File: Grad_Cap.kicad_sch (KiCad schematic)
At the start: 2 parts, among them U1 Itsy_NRF

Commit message: update part
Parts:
- U1: footprint (none) -> Package_DIP:DIP-28_W15.24mm_LongPads
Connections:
- net GND: now also U1.27 (GND); no longer U1. (VHI)
- net VBUS: now also U1.28 (VBAT); no longer U1. (VHI)
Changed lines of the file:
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@@
     (property "Reference" "U1" (id 0) (at 40.64 19.05 0))
     (property "Value" "Itsy_NRF" (id 1) (at 40.64 21.59 0))
-    (property "Footprint" "" (id 2) (at 29.21 26.67 0)
+    (property "Footprint" "Package_DIP:DIP-28_W15.24mm_LongPads" (id 2) (at 29.21 26.67 0)
       (effects (font (size 1.27 1.27)) hide)
     )
@@
       (effects (font (size 1.27 1.27)) hide)
     )
-    (pin "")
-    (pin "")
-    (pin "")
-    (pin "")
-    (pin "")
-    (pin "")
-    (pin "")
-    (pin "")
-    (pin "")
-    (pin "")
-    (pin "")
-    (pin "")
-    (pin "")
-    (pin "")
-    (pin "")
-    (pin "")
-    (pin "")
-    (pin "")
-    (pin "")
-    (pin "")
-    (pin "")
-    (pin "")
-    (pin "")
-    (pin "")
-    (pin "")
-    (pin "")
-    (pin "")
-    (pin "")
+    (pin "1")
+    (pin "10")
+    (pin "11")
+    (pin "12")
+    (pin "13")
+    (pin "14")
+    (pin "15")
+    (pin "16")
+    (pin "17")
+    (pin "18")
+    (pin "19")
+    (pin "2")
+    (pin "20")
+    (pin "21")
+    (pin "22")
+    (pin "23")
+    (pin "24")
+    (pin "25")
+    (pin "26")
+    (pin "27")
+    (pin "28")
+    (pin "3")
+    (pin "4")
+    (pin "5")
+    (pin "6")
+    (pin "7")
+    (pin "8")
+    (pin "9")
   )
   (symbol (lib_id "LED:Inolux_IN-PI554FCH") (at 147.32 31.75 0) (unit 1)
@@
     )
     (path "/a5c46b29-3091-45c4-b411-8345b67a7d70"
-      (reference "U1") (unit 1) (value "Itsy_NRF") (footprint "")
+      (reference "U1") (unit 1) (value "Itsy_NRF") (footprint "Package_DIP:DIP-28_W15.24mm_LongPads")
     )
   )

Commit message: Cleaning files
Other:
- company: (none) -> Lala
- title: (none) -> Graduation Cap
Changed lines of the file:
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@@
 (kicad_sch (version 20211123) (generator eeschema)
   (paper "A4")
+  (title_block
+    (title "Graduation Cap")
+    (date "2022-12-23")
+    (rev "1.0")
+    (company "Lala")
+  )
   (wire (pts (xy 147.32 39.37) (xy 147.32 40.64))
     (stroke (width 0) (type default) (color 0 0 0 0))

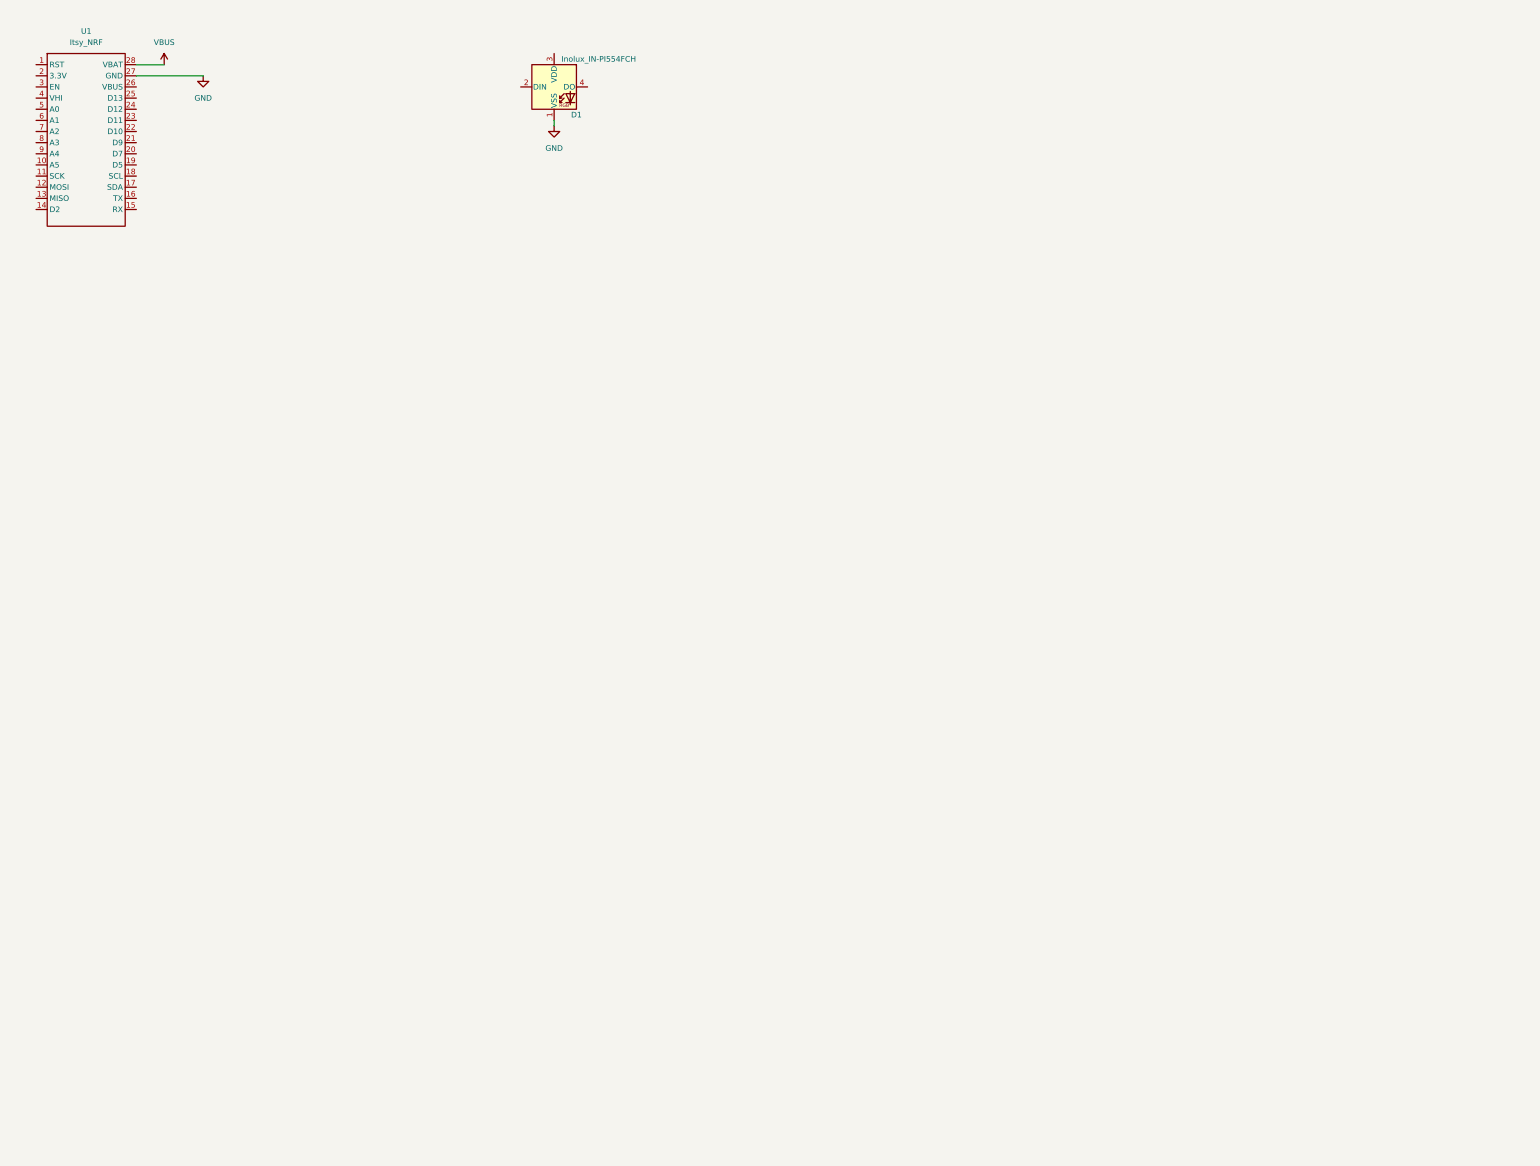
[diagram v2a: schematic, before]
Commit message: Added neopixels
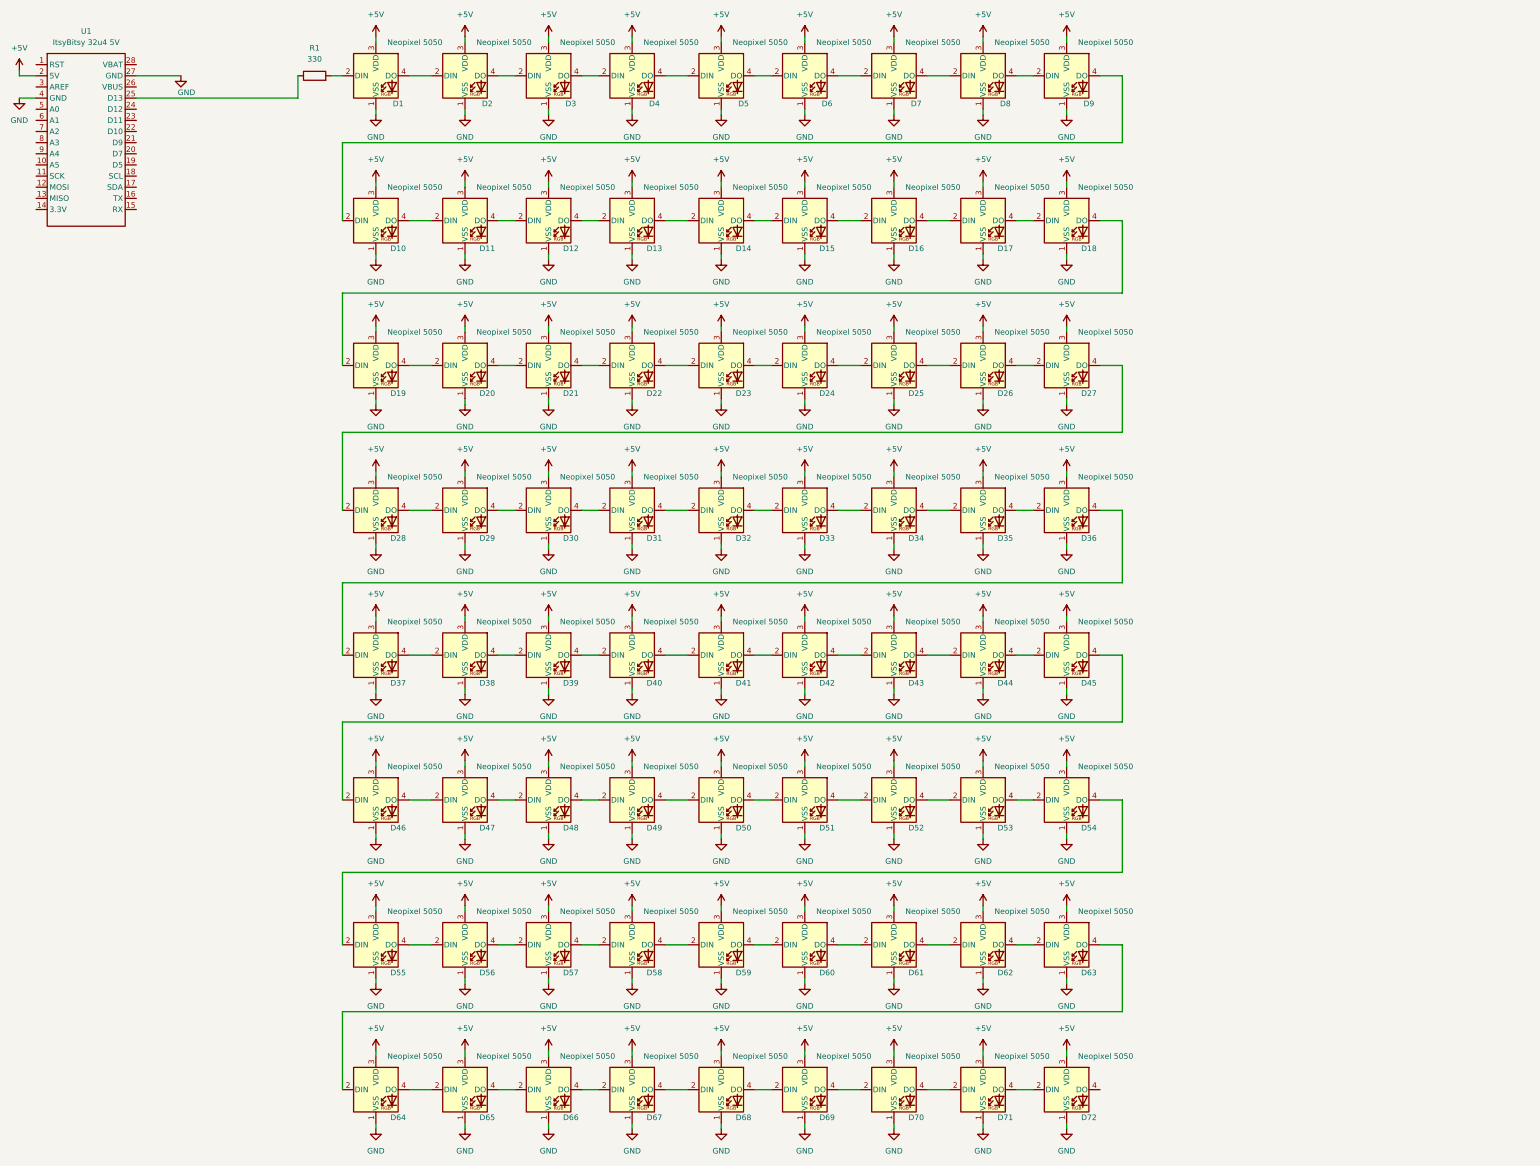
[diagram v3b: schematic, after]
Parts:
- added D10, D11, D12, D13, D14, D15, D16, D17, D18, D19, D2, D20, D21, D22, D23, D24, D25, D26, D27, D28, D29, D3, D30, D31, D32, D33, D34, D35, D36, D37, D38, D39, D4, D40, D41, D42, D43, D44, D45, D46, D47, D48, D49, D5, D50, D51, D52, D53, D54, D55, D56, D57, D58, D59, D6, D60, D61, D62, D63, D64, D65, D66, D67, D68, D69, D7, D70, D71, D72, D8, D9: Neopixel 5050, LED_SMD:LED_Inolux_IN-PI554FCH_PLCC4_5.0x5.0mm_P3.2mm, symbol LED:Inolux_IN-PI554FCH
- added R1: 330, Resistor_SMD:R_1206_3216Metric_Pad1.30x1.75mm_HandSolder, symbol Device:R
- D1: value Inolux_IN-PI554FCH -> Neopixel 5050
- U1: value Itsy_NRF -> ItsyBitsy 32u4 5V
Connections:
- net GND: now also U1.4 (GND), D10.1 (VSS), D11.1 (VSS), D12.1 (VSS), D13.1 (VSS), D14.1 (VSS), D15.1 (VSS), D16.1 (VSS), D17.1 (VSS), D18.1 (VSS), D19.1 (VSS), D2.1 (VSS), D20.1 (VSS), D21.1 (VSS), D22.1 (VSS), D23.1 (VSS), D24.1 (VSS), D25.1 (VSS), D26.1 (VSS), D27.1 (VSS), D28.1 (VSS), D29.1 (VSS), D3.1 (VSS), D30.1 (VSS), D31.1 (VSS), D32.1 (VSS), D33.1 (VSS), D34.1 (VSS), D35.1 (VSS), D36.1 (VSS), D37.1 (VSS), D38.1 (VSS), D39.1 (VSS), D4.1 (VSS), D40.1 (VSS), D41.1 (VSS), D42.1 (VSS), D43.1 (VSS), D44.1 (VSS), D45.1 (VSS), D46.1 (VSS), D47.1 (VSS), D48.1 (VSS), D49.1 (VSS), D5.1 (VSS), D50.1 (VSS), D51.1 (VSS), D52.1 (VSS), D53.1 (VSS), D54.1 (VSS), D55.1 (VSS), D56.1 (VSS), D57.1 (VSS), D58.1 (VSS), D59.1 (VSS), D6.1 (VSS), D60.1 (VSS), D61.1 (VSS), D62.1 (VSS), D63.1 (VSS), D64.1 (VSS), D65.1 (VSS), D66.1 (VSS), D67.1 (VSS), D68.1 (VSS), D69.1 (VSS), D7.1 (VSS), D70.1 (VSS), D71.1 (VSS), D72.1 (VSS), D8.1 (VSS), D9.1 (VSS)
- net +5V: now reaches U1.2 (5V)
- net +5V: now also D1.3 (VDD), D10.3 (VDD), D11.3 (VDD), D12.3 (VDD), D13.3 (VDD), D14.3 (VDD), D15.3 (VDD), D16.3 (VDD), D17.3 (VDD), D18.3 (VDD), D19.3 (VDD), D2.3 (VDD), D20.3 (VDD), D21.3 (VDD), D22.3 (VDD), D23.3 (VDD), D24.3 (VDD), D25.3 (VDD), D26.3 (VDD), D27.3 (VDD), D28.3 (VDD), D29.3 (VDD), D3.3 (VDD), D30.3 (VDD), D31.3 (VDD), D32.3 (VDD), D33.3 (VDD), D34.3 (VDD), D35.3 (VDD), D36.3 (VDD), D37.3 (VDD), D38.3 (VDD), D39.3 (VDD), D4.3 (VDD), D40.3 (VDD), D41.3 (VDD), D42.3 (VDD), D43.3 (VDD), D44.3 (VDD), D45.3 (VDD), D46.3 (VDD), D47.3 (VDD), D48.3 (VDD), D49.3 (VDD), D5.3 (VDD), D50.3 (VDD), D51.3 (VDD), D52.3 (VDD), D53.3 (VDD), D54.3 (VDD), D55.3 (VDD), D56.3 (VDD), D57.3 (VDD), D58.3 (VDD), D59.3 (VDD), D6.3 (VDD), D60.3 (VDD), D61.3 (VDD), D62.3 (VDD), D63.3 (VDD), D64.3 (VDD), D65.3 (VDD), D66.3 (VDD), D67.3 (VDD), D68.3 (VDD), D69.3 (VDD), D7.3 (VDD), D70.3 (VDD), D71.3 (VDD), D72.3 (VDD), D8.3 (VDD), D9.3 (VDD)
- net at U1.25 (D13): now also R1.1
- net at D1.2 (DIN): now also R1.2
- net at D1.4 (DO): now also D2.2 (DIN)
- net VBUS: no longer names the net of U1.28 (VBAT)
- new net: D35.4 (DO), D36.2 (DIN)
- new net: D36.4 (DO), D37.2 (DIN)
- new net: D59.4 (DO), D60.2 (DIN)
- new net: D60.4 (DO), D61.2 (DIN)
- new net: D39.4 (DO), D40.2 (DIN)
- new net: D40.4 (DO), D41.2 (DIN)
- new net: D62.4 (DO), D63.2 (DIN)
- new net: D63.4 (DO), D64.2 (DIN)
- new net: D56.4 (DO), D57.2 (DIN)
- new net: D57.4 (DO), D58.2 (DIN)
- new net: D18.4 (DO), D19.2 (DIN)
- new net: D19.4 (DO), D20.2 (DIN)
- new net: D54.4 (DO), D55.2 (DIN)
- new net: D55.4 (DO), D56.2 (DIN)
- new net: D37.4 (DO), D38.2 (DIN)
- new net: D38.4 (DO), D39.2 (DIN)
- new net: D29.4 (DO), D30.2 (DIN)
- new net: D30.4 (DO), D31.2 (DIN)
- new net: D58.4 (DO), D59.2 (DIN)
- new net: D22.4 (DO), D23.2 (DIN)
- new net: D23.4 (DO), D24.2 (DIN)
- new net: D47.4 (DO), D48.2 (DIN)
- new net: D48.4 (DO), D49.2 (DIN)
- new net: D20.4 (DO), D21.2 (DIN)
- new net: D21.4 (DO), D22.2 (DIN)
- new net: D49.4 (DO), D50.2 (DIN)
- new net: D44.4 (DO), D45.2 (DIN)
- new net: D45.4 (DO), D46.2 (DIN)
- new net: D31.4 (DO), D32.2 (DIN)
- new net: D2.4 (DO), D3.2 (DIN)
- new net: D3.4 (DO), D4.2 (DIN)
- new net: D11.4 (DO), D12.2 (DIN)
- new net: D12.4 (DO), D13.2 (DIN)
- new net: D4.4 (DO), D5.2 (DIN)
- new net: D5.4 (DO), D6.2 (DIN)
- new net: D26.4 (DO), D27.2 (DIN)
- new net: D27.4 (DO), D28.2 (DIN)
- new net: D70.4 (DO), D71.2 (DIN)
- new net: D71.4 (DO), D72.2 (DIN)
- new net: D42.4 (DO), D43.2 (DIN)
- new net: D43.4 (DO), D44.2 (DIN)
- new net: D17.4 (DO), D18.2 (DIN)
- new net: D6.4 (DO), D7.2 (DIN)
- new net: D61.4 (DO), D62.2 (DIN)
- new net: D66.4 (DO), D67.2 (DIN)
- new net: D67.4 (DO), D68.2 (DIN)
- new net: D65.4 (DO), D66.2 (DIN)
- new net: D10.2 (DIN), D9.4 (DO)
- new net: D10.4 (DO), D11.2 (DIN)
- new net: D33.4 (DO), D34.2 (DIN)
- new net: D34.4 (DO), D35.2 (DIN)
- new net: D7.4 (DO), D8.2 (DIN)
- new net: D32.4 (DO), D33.2 (DIN)
- new net: D68.4 (DO), D69.2 (DIN)
- new net: D69.4 (DO), D70.2 (DIN)
- new net: D52.4 (DO), D53.2 (DIN)
- new net: D53.4 (DO), D54.2 (DIN)
- new net: D50.4 (DO), D51.2 (DIN)
- new net: D28.4 (DO), D29.2 (DIN)
- new net: D41.4 (DO), D42.2 (DIN)
- new net: D24.4 (DO), D25.2 (DIN)
- new net: D25.4 (DO), D26.2 (DIN)
- new net: D8.4 (DO), D9.2 (DIN)
- new net: D15.4 (DO), D16.2 (DIN)
- new net: D16.4 (DO), D17.2 (DIN)
- new net: D51.4 (DO), D52.2 (DIN)
- new net: D64.4 (DO), D65.2 (DIN)
- new net: D46.4 (DO), D47.2 (DIN)
- new net: D13.4 (DO), D14.2 (DIN)
- new net: D14.4 (DO), D15.2 (DIN)
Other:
- moved on the sheet: D1

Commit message: routing time
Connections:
- net at R1.1: now also U1.19 (D5); no longer U1.25 (D13)
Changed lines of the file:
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@@
     (stroke (width 0) (type default) (color 0 0 0 0))
   )
-  (wire (pts (xy 88.9 34.29) (xy 88.9 29.21))
+  (wire (pts (xy 88.9 29.21) (xy 88.9 49.53))
     (stroke (width 0) (type default) (color 0 0 0 0))
   )
@@
     (stroke (width 0) (type default) (color 0 0 0 0))
   )
+  (wire (pts (xy 88.9 49.53) (xy 52.07 49.53))
+    (stroke (width 0) (type default) (color 0 0 0 0))
+  )
   (wire (pts (xy 276.86 161.29) (xy 271.78 161.29))
     (stroke (width 0) (type default) (color 0 0 0 0))
@@
     (stroke (width 0) (type default) (color 0 0 0 0))
   )
-  (wire (pts (xy 52.07 34.29) (xy 88.9 34.29))
-    (stroke (width 0) (type default) (color 0 0 0 0))
-  )

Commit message: ground vias?
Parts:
- removed D37: Neopixel 5050, LED_SMD:LED_Inolux_IN-PI554FCH_PLCC4_5.0x5.0mm_P3.2mm, symbol LED:Inolux_IN-PI554FCH
- added D73, D74, D75, D76, D77, D78, D79, D80, D81, D82, D83, D84, D85: Neopixel 5050, LED_SMD:LED_Inolux_IN-PI554FCH_PLCC4_5.0x5.0mm_P3.2mm, symbol LED:Inolux_IN-PI554FCH
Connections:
- net +5V: now also D73.3 (VDD), D74.3 (VDD), D75.3 (VDD), D76.3 (VDD), D77.3 (VDD), D78.3 (VDD), D79.3 (VDD), D80.3 (VDD), D81.3 (VDD), D82.3 (VDD), D83.3 (VDD), D84.3 (VDD), D85.3 (VDD)
- net GND: now also D73.1 (VSS), D74.1 (VSS), D75.1 (VSS), D76.1 (VSS), D77.1 (VSS), D78.1 (VSS), D79.1 (VSS), D80.1 (VSS), D81.1 (VSS), D82.1 (VSS), D83.1 (VSS), D84.1 (VSS), D85.1 (VSS)
- net at D36.4 (DO): now also D38.2 (DIN)
- net at D72.4 (DO): now also D73.2 (DIN)
- new net: D75.4 (DO), D76.2 (DIN)
- new net: D76.4 (DO), D77.2 (DIN)
- new net: D82.4 (DO), D83.2 (DIN)
- new net: D83.4 (DO), D84.2 (DIN)
- new net: D84.4 (DO), D85.2 (DIN)
- new net: D74.4 (DO), D75.2 (DIN)
- new net: D79.4 (DO), D80.2 (DIN)
- new net: D80.4 (DO), D81.2 (DIN)
- new net: D78.4 (DO), D79.2 (DIN)
- new net: D73.4 (DO), D74.2 (DIN)
- new net: D77.4 (DO), D78.2 (DIN)
- new net: D81.4 (DO), D82.2 (DIN)

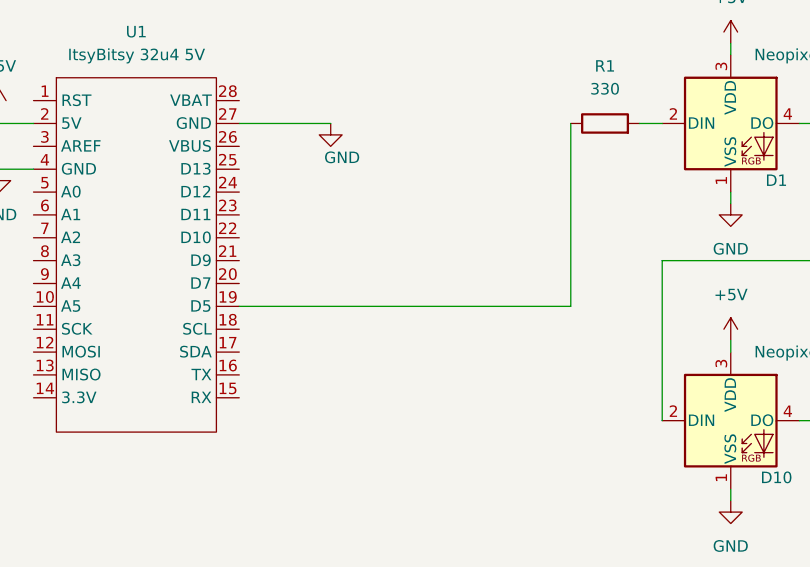
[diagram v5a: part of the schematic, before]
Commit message: Routing and pours done
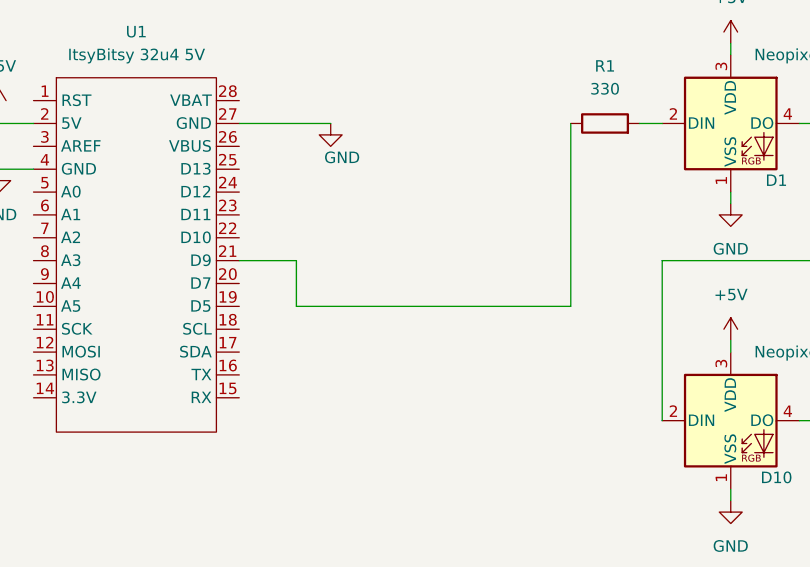
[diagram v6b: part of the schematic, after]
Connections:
- net at R1.1: now also U1.21 (D9); no longer U1.19 (D5)
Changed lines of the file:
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@@
+    (stroke (width 0) (type default) (color 0 0 0 0))
+  )
+  (wire (pts (xy 52.07 44.45) (xy 58.42 44.45))
     (stroke (width 0) (type default) (color 0 0 0 0))
   )
@@
     (stroke (width 0) (type default) (color 0 0 0 0))
   )
+  (wire (pts (xy 58.42 44.45) (xy 58.42 49.53))
+    (stroke (width 0) (type default) (color 0 0 0 0))
+  )
   (wire (pts (xy 323.85 219.71) (xy 323.85 41.91))
     (stroke (width 0) (type default) (color 0 0 0 0))
@@
     (stroke (width 0) (type default) (color 0 0 0 0))
   )
-  (wire (pts (xy 88.9 49.53) (xy 52.07 49.53))
-    (stroke (width 0) (type default) (color 0 0 0 0))
-  )
+  (wire (pts (xy 88.9 49.53) (xy 58.42 49.53))
+    (stroke (width 0) (type default) (color 0 0 0 0))
+  )
